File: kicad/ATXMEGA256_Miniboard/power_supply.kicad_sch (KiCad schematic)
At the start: 14 parts, among them J1 1x2 Screw Terminal, J15 1x3 Goldpin Header, J6 1x2 Goldpin Header, J7 1x2 Goldpin Header, J8 1x3 Goldpin Header, Q1 MMFTP3334K, U2 MCP1703A-3302E/DB

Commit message: Zmiana zlacza PDI, dodany makefile i struktura plikow
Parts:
- renumbered C12 to C14, C13 to C15, C14 to C16, J15 to J4, J6 to J5, J7 to J6, J8 to J7, J1 to J8
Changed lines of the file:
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@@
 		(dnp no)
 		(fields_autoplaced yes)
-		(property "Reference" "#PWR020"
+		(property "Reference" "#PWR023"
 			(at 135.89 116.84 0)
 			(effects
@@
 			(project "ATXMEGA256_Miniboard"
 				(path "/ef1e5883-c6cf-4bad-8eaa-8ec9109f9d71/1d37de11-1936-4242-b544-634b362ae3ca"
-					(reference "#PWR020")
+					(reference "#PWR023")
 					(unit 1)
 				)
@@
 		(on_board yes)
 		(dnp no)
-		(property "Reference" "C13"
+		(property "Reference" "C15"
 			(at 157.48 99.06 0)
 			(effects
@@
 			(project "ATXMEGA256_Miniboard"
 				(path "/ef1e5883-c6cf-4bad-8eaa-8ec9109f9d71/1d37de11-1936-4242-b544-634b362ae3ca"
-					(reference "C13")
+					(reference "C15")
 					(unit 1)
 				)
@@
 		(on_board yes)
 		(dnp no)
-		(property "Reference" "C14"
+		(property "Reference" "C16"
 			(at 241.3 99.06 0)
 			(effects
@@
 			(project "ATXMEGA256_Miniboard"
 				(path "/ef1e5883-c6cf-4bad-8eaa-8ec9109f9d71/1d37de11-1936-4242-b544-634b362ae3ca"
-					(reference "C14")
+					(reference "C16")
 					(unit 1)
 				)
@@
 		(dnp no)
 		(fields_autoplaced yes)
-		(property "Reference" "#PWR035"
+		(property "Reference" "#PWR018"
 			(at 220.98 80.01 0)
 			(effects
@@
 			(project "ATXMEGA256_Miniboard"
 				(path "/ef1e5883-c6cf-4bad-8eaa-8ec9109f9d71/1d37de11-1936-4242-b544-634b362ae3ca"
-					(reference "#PWR035")
+					(reference "#PWR018")
 					(unit 1)
 				)
@@
 		(dnp no)
 		(fields_autoplaced yes)
-		(property "Reference" "J6"
+		(property "Reference" "J5"
 			(at 199.39 84.455 90)
 			(effects
@@
 			(project "ATXMEGA256_Miniboard"
 				(path "/ef1e5883-c6cf-4bad-8eaa-8ec9109f9d71/1d37de11-1936-4242-b544-634b362ae3ca"
-					(reference "J6")
+					(reference "J5")
 					(unit 1)
 				)
@@
 		(on_board yes)
 		(dnp no)
-		(property "Reference" "C12"
+		(property "Reference" "C14"
 			(at 119.38 99.06 0)
 			(effects
@@
 			(project "ATXMEGA256_Miniboard"
 				(path "/ef1e5883-c6cf-4bad-8eaa-8ec9109f9d71/1d37de11-1936-4242-b544-634b362ae3ca"
-					(reference "C12")
+					(reference "C14")
 					(unit 1)
 				)
@@
 		(dnp no)
 		(fields_autoplaced yes)
-		(property "Reference" "J7"
+		(property "Reference" "J6"
 			(at 245.11 84.455 90)
 			(effects
@@
 			(project "ATXMEGA256_Miniboard"
 				(path "/ef1e5883-c6cf-4bad-8eaa-8ec9109f9d71/1d37de11-1936-4242-b544-634b362ae3ca"
-					(reference "J7")
+					(reference "J6")
 					(unit 1)
 				)
@@
 		(dnp no)
 		(fields_autoplaced yes)
-		(property "Reference" "J8"
+		(property "Reference" "J7"
 			(at 76.835 83.82 0)
 			(effects
@@
 			(project "ATXMEGA256_Miniboard"
 				(path "/ef1e5883-c6cf-4bad-8eaa-8ec9109f9d71/1d37de11-1936-4242-b544-634b362ae3ca"
-					(reference "J8")
+					(reference "J7")
 					(unit 1)
 				)
@@
 		(dnp no)
 		(fields_autoplaced yes)
-		(property "Reference" "#PWR022"
+		(property "Reference" "#PWR025"
 			(at 175.26 116.84 0)
 			(effects
@@
 			(project "ATXMEGA256_Miniboard"
 				(path "/ef1e5883-c6cf-4bad-8eaa-8ec9109f9d71/1d37de11-1936-4242-b544-634b362ae3ca"
-					(reference "#PWR022")
+					(reference "#PWR025")
 					(unit 1)
 				)
@@
 		(dnp no)
 		(fields_autoplaced yes)
-		(property "Reference" "J1"
+		(property "Reference" "J8"
 			(at 77.47 97.79 0)
 			(effects
@@
 			(project "ATXMEGA256_Miniboard"
 				(path "/ef1e5883-c6cf-4bad-8eaa-8ec9109f9d71/1d37de11-1936-4242-b544-634b362ae3ca"
-					(reference "J1")
+					(reference "J8")
 					(unit 1)
 				)
@@
 		(on_board yes)
 		(dnp no)
-		(property "Reference" "#PWR01"
+		(property "Reference" "#PWR020"
 			(at 88.9 116.84 0)
 			(effects
@@
 			(project "ATXMEGA256_Miniboard"
 				(path "/ef1e5883-c6cf-4bad-8eaa-8ec9109f9d71/1d37de11-1936-4242-b544-634b362ae3ca"
-					(reference "#PWR01")
+					(reference "#PWR020")
 					(unit 1)
 				)
@@
 		(dnp no)
 		(fields_autoplaced yes)
-		(property "Reference" "#PWR019"
+		(property "Reference" "#PWR022"
 			(at 115.57 116.84 0)
 			(effects
@@
 			(project "ATXMEGA256_Miniboard"
 				(path "/ef1e5883-c6cf-4bad-8eaa-8ec9109f9d71/1d37de11-1936-4242-b544-634b362ae3ca"
-					(reference "#PWR019")
+					(reference "#PWR022")
 					(unit 1)
 				)
@@
 		(dnp no)
 		(fields_autoplaced yes)
-		(property "Reference" "#PWR023"
+		(property "Reference" "#PWR026"
 			(at 237.49 116.84 0)
 			(effects
@@
 			(project "ATXMEGA256_Miniboard"
 				(path "/ef1e5883-c6cf-4bad-8eaa-8ec9109f9d71/1d37de11-1936-4242-b544-634b362ae3ca"
-					(reference "#PWR023")
+					(reference "#PWR026")
 					(unit 1)
 				)
@@
 		(dnp no)
 		(fields_autoplaced yes)
-		(property "Reference" "#PWR041"
+		(property "Reference" "#PWR017"
 			(at 175.26 80.01 0)
 			(effects
@@
 			(project "ATXMEGA256_Miniboard"
 				(path "/ef1e5883-c6cf-4bad-8eaa-8ec9109f9d71/1d37de11-1936-4242-b544-634b362ae3ca"
-					(reference "#PWR041")
+					(reference "#PWR017")
 					(unit 1)
 				)
@@
 		(dnp no)
 		(fields_autoplaced yes)
-		(property "Reference" "J15"
+		(property "Reference" "J4"
 			(at 162.56 76.2 90)
 			(effects
@@
 			(project "ATXMEGA256_Miniboard"
 				(path "/ef1e5883-c6cf-4bad-8eaa-8ec9109f9d71/1d37de11-1936-4242-b544-634b362ae3ca"
-					(reference "J15")
+					(reference "J4")
 					(unit 1)
 				)
@@
 		(dnp no)
 		(fields_autoplaced yes)
-		(property "Reference" "#PWR034"
+		(property "Reference" "#PWR019"
 			(at 265.43 80.01 0)
 			(effects
@@
 			(project ""
 				(path "/ef1e5883-c6cf-4bad-8eaa-8ec9109f9d71/1d37de11-1936-4242-b544-634b362ae3ca"
-					(reference "#PWR034")
+					(reference "#PWR019")
 					(unit 1)
 				)
@@
 		(dnp no)
 		(fields_autoplaced yes)
-		(property "Reference" "#PWR018"
+		(property "Reference" "#PWR021"
 			(at 102.87 116.84 0)
 			(effects
@@
 			(project "ATXMEGA256_Miniboard"
 				(path "/ef1e5883-c6cf-4bad-8eaa-8ec9109f9d71/1d37de11-1936-4242-b544-634b362ae3ca"
-					(reference "#PWR018")
+					(reference "#PWR021")
 					(unit 1)
 				)
@@
 		(dnp no)
 		(fields_autoplaced yes)
-		(property "Reference" "#PWR021"
+		(property "Reference" "#PWR024"
 			(at 153.67 116.84 0)
 			(effects
@@
 			(project "ATXMEGA256_Miniboard"
 				(path "/ef1e5883-c6cf-4bad-8eaa-8ec9109f9d71/1d37de11-1936-4242-b544-634b362ae3ca"
-					(reference "#PWR021")
-					(unit 1)
-				)
+					(reference "#PWR024")
+					(unit 1)
+				)

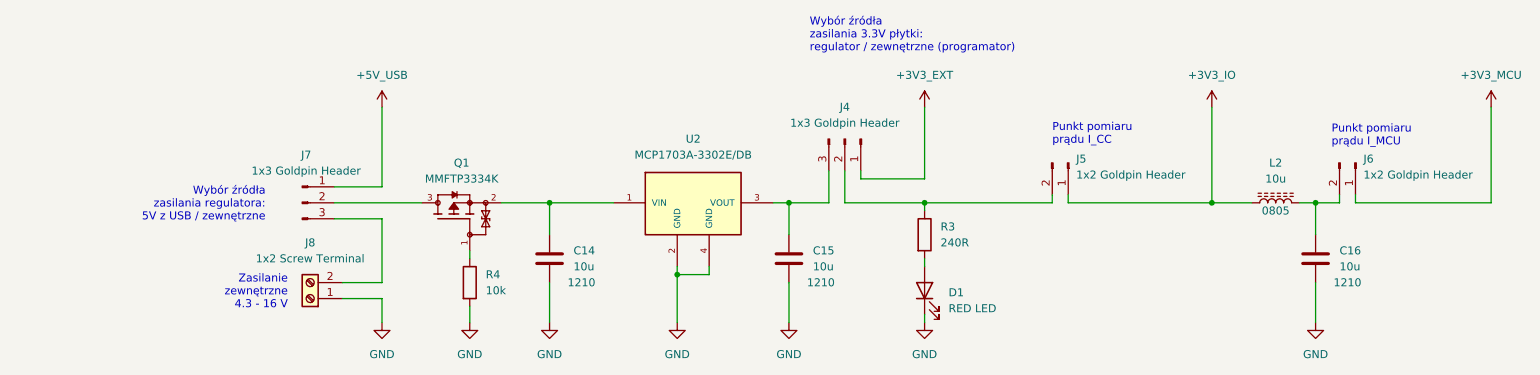
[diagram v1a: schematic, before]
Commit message: layout komponentów
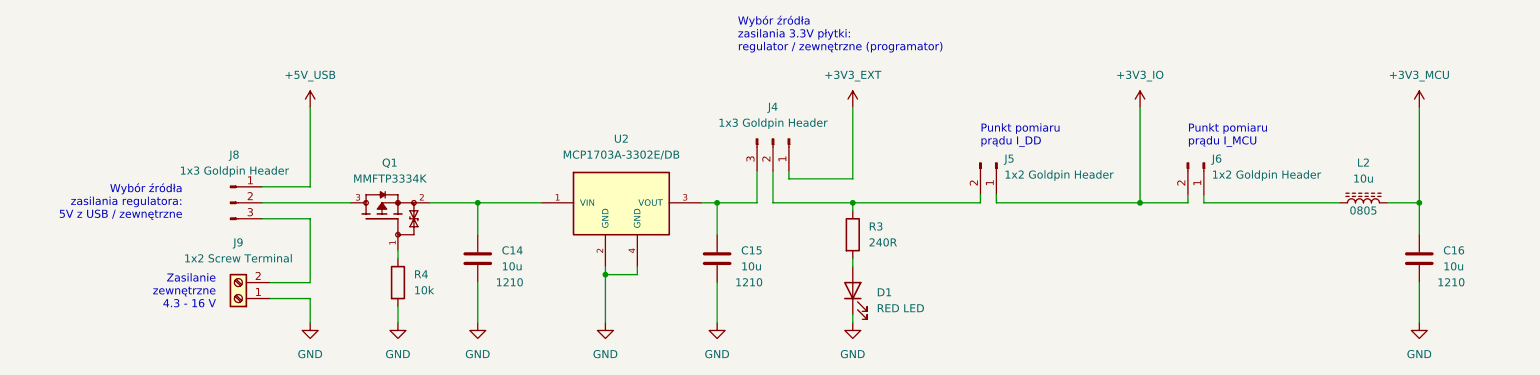
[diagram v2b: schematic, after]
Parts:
- J9: renamed from J8; footprint TerminalBlock:TerminalBlock_bornier-2_P5.08mm -> DG381-3.5-02P-13-00AH:DG381-3.5-02P-13-00AH
- renumbered J7 to J8
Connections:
- net +3V3_IO: now also J6.2 (Pin_2); no longer L2.1
- net +3V3_MCU: now also C16.2, L2.2; no longer J6.1 (Pin_1)
- new net: J6.1 (Pin_1), L2.1
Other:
- note added: "Punkt pomiaru prądu I_DD"
- note removed: "Punkt pomiaru prądu I_CC"
- moved on the sheet: C14, C15, C16, D1, J4, J5, J6, J8, J9, L2, Q1, R3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

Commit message: update BOM, poprawki masy
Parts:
- Q1: Manufacturer (none) -> DIOTEC SEMICONDUCTOR; Manufacturet DIOTEC SEMICONDUCTOR -> (none)
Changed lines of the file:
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@@
 			)
 		)
-		(property "Manufacturet" "DIOTEC SEMICONDUCTOR"
+		(property "Manufacturer" "DIOTEC SEMICONDUCTOR"
 			(at 80.772 77.724 0)
 			(effects
